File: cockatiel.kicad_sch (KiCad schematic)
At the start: 40 parts, among them J1 Programmer, J10 MIC_N_BYP, J11 MIC_P_SEL, J12 MIC_N_SEL, J13 Cox Box Mic In, J14 Cox Box Mic Out, J15 Mic Out, J16 Headset/Mic In, J3 DEBUG_UART, J4 RESET, J5 Magnetic connector, J6 PWR, J7 Battery Connector, J8 LED, J9 MIC_P_BYP, T1 Transformer_Audio, U1 F-3188_CSR8645

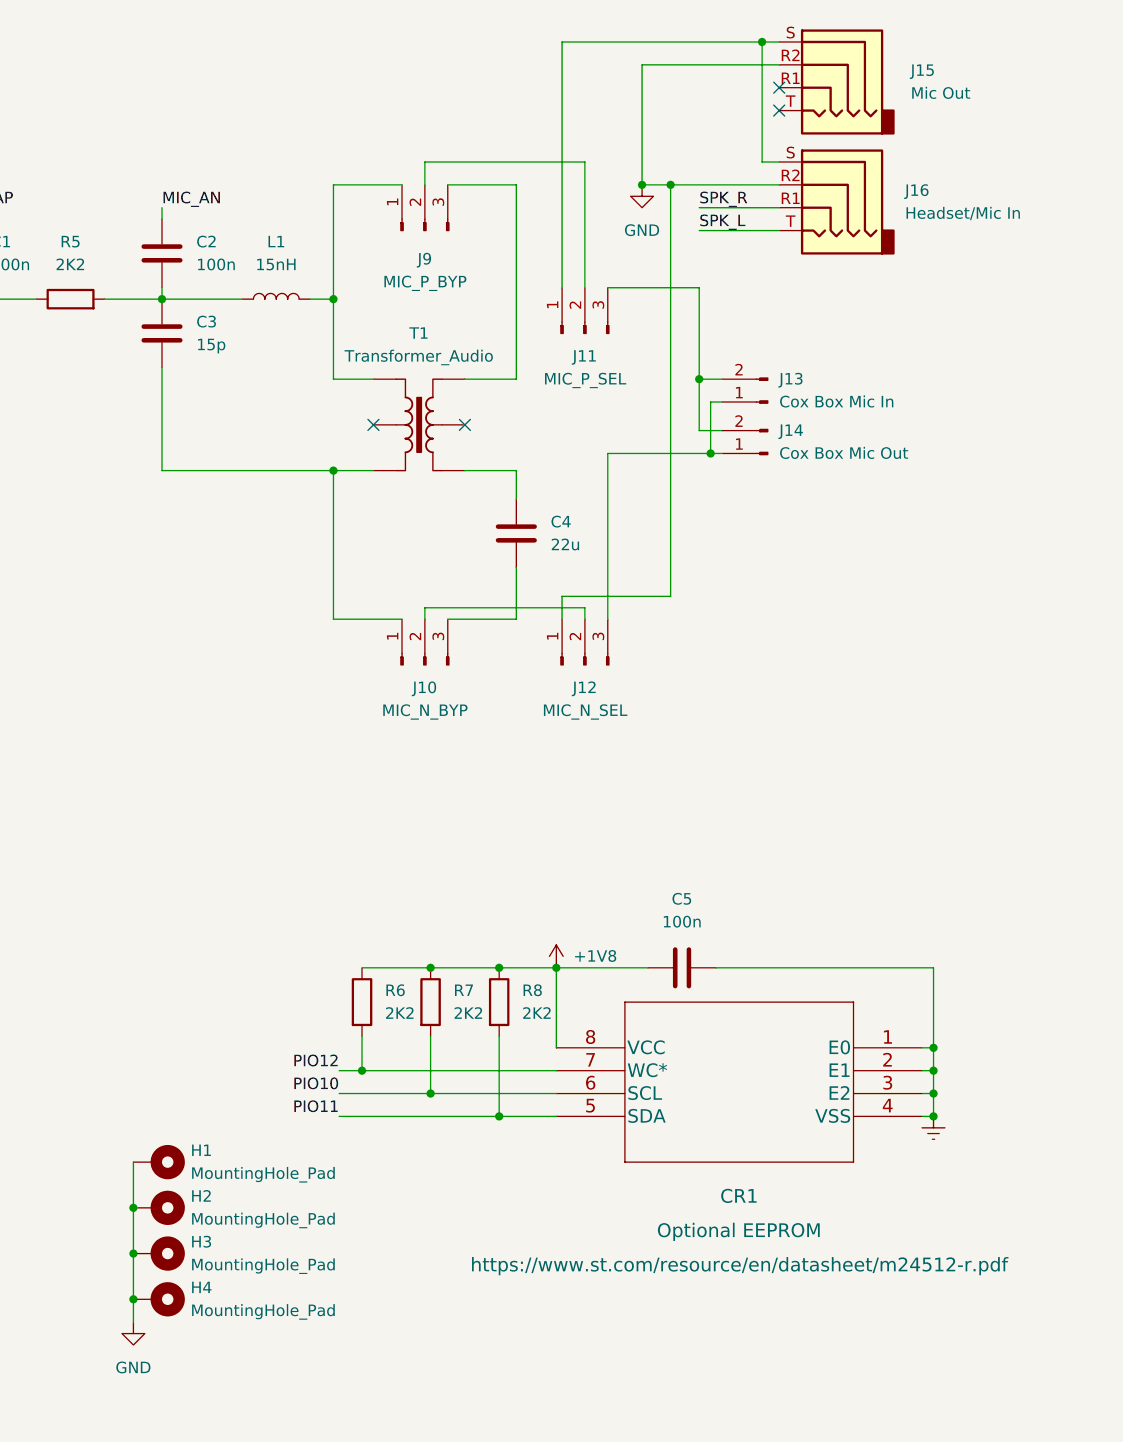
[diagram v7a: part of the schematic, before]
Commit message: WIP: reduce the board complexity and size
This in turn reduces the eBoM and board size, aiming to reduce cost of
manufacture.
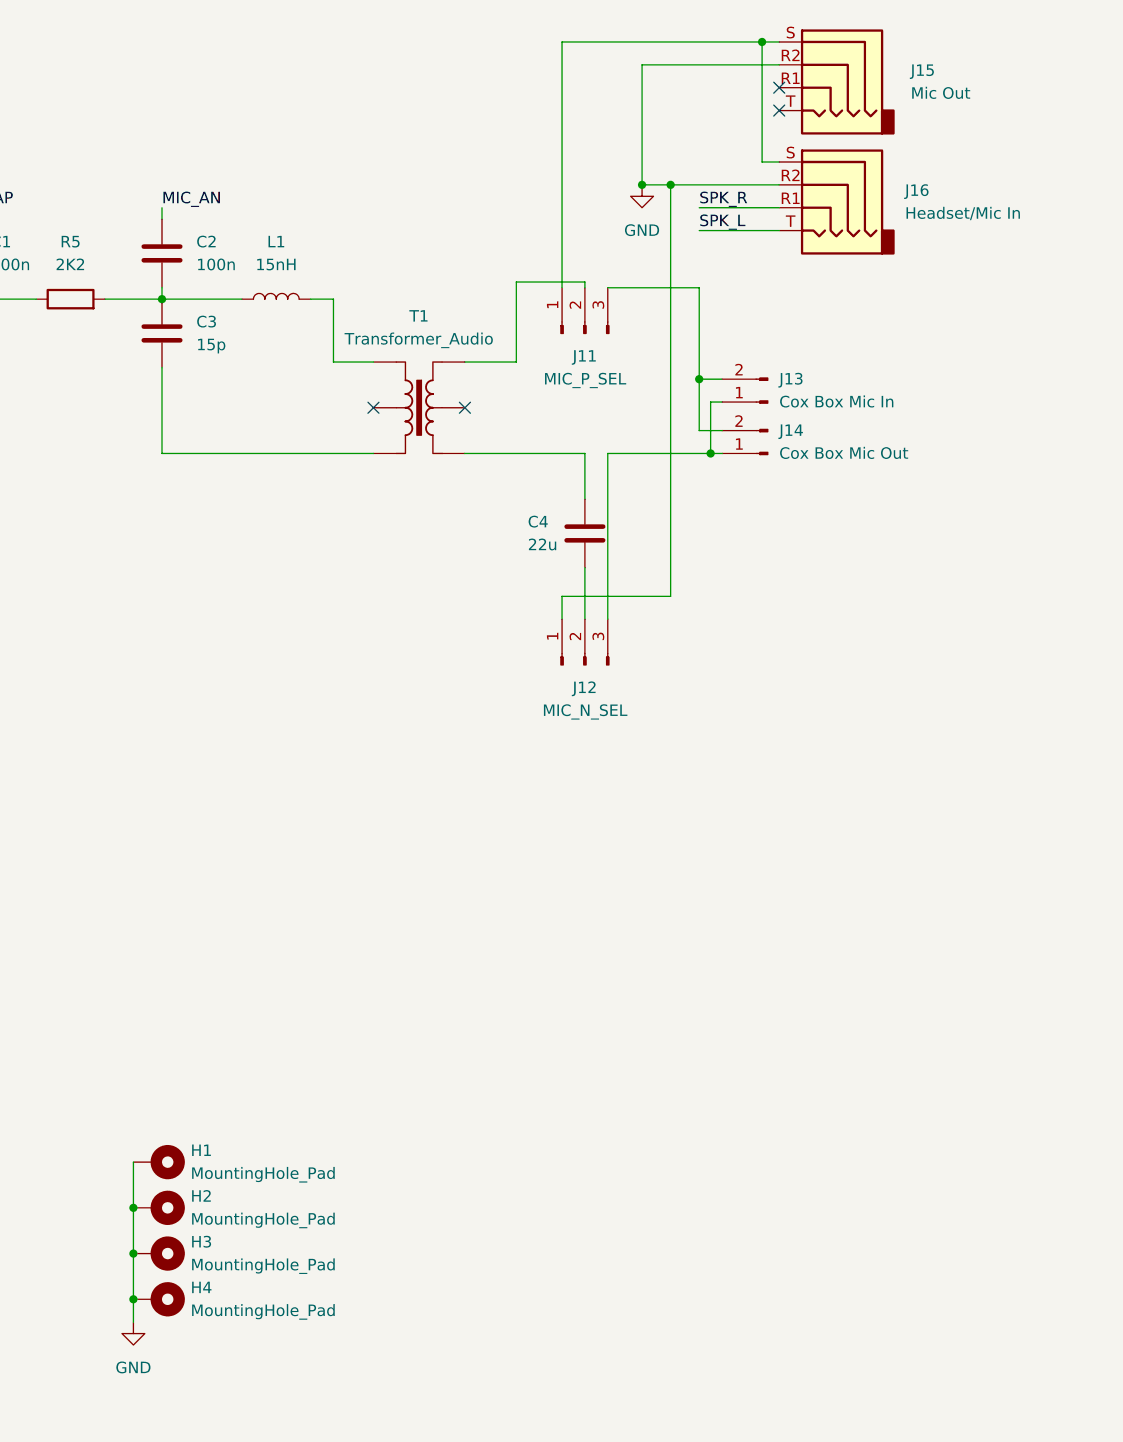
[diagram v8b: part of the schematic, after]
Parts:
- removed C5: 100n, Capacitor_SMD:C_0805_2012Metric_Pad1.18x1.45mm_HandSolder, symbol Device:C
- removed CR1: Optional EEPROM, st:M24512-RMN6P, symbol 2022-08-27_17-15-02:M24512-RMN6P
- removed J10: MIC_N_BYP, Connector_PinHeader_2.54mm:PinHeader_1x03_P2.54mm_Vertical, symbol Connector:Conn_01x03_Male
- removed J9: MIC_P_BYP, Connector_PinHeader_2.54mm:PinHeader_1x03_P2.54mm_Vertical, symbol Connector:Conn_01x03_Male
- removed R6, R7, R8: 2K2, Resistor_SMD:R_0805_2012Metric_Pad1.20x1.40mm_HandSolder, symbol Device:R
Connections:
- net at J12.2 (Pin_2): now also C4.2
- net at T1.1: now also J11.2 (Pin_2)
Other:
- moved on the sheet: C4, T1
